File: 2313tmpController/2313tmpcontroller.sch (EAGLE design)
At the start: 32 parts, among them IC1 AT90S2313P, T1 BD139, T2 BD139, T3 BD139, T4 BD139

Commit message: fixed some pads
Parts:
- GNDIN, RSTBTN, VCCIN: device pinhead:PINHD-1X1 -> wirepad:2,54/0,8
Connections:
- net GND: now also GNDIN.P; no longer GNDIN.1
- net N$19: now also RSTBTN.P; no longer RSTBTN.1
- net VCC: now also VCCIN.P; no longer VCCIN.1
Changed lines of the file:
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@@
 <part name="T3" library="transistor" deviceset="BD139" device=""/>
 <part name="T4" library="transistor" deviceset="BD139" device=""/>
-<part name="RSTBTN" library="pinhead" deviceset="PINHD-1X1" device=""/>
 <part name="R5" library="rcl" deviceset="R-EU_" device="0207/7"/>
-<part name="VCCIN" library="pinhead" deviceset="PINHD-1X1" device=""/>
-<part name="GNDIN" library="pinhead" deviceset="PINHD-1X1" device=""/>
 <part name="PAD1" library="wirepad" deviceset="WIREPAD" device="2,15/1,0"/>
 <part name="PAD2" library="wirepad" deviceset="WIREPAD" device="2,15/1,0"/>
@@
 <part name="R6" library="rcl" deviceset="R-EU_" device="0207/7"/>
 <part name="LED1" library="led" deviceset="LED" device="B153"/>
+<part name="VCCIN" library="wirepad" deviceset="2,54/0,8" device=""/>
+<part name="GNDIN" library="wirepad" deviceset="2,54/0,8" device=""/>
+<part name="RSTBTN" library="wirepad" deviceset="2,54/0,8" device=""/>
 </parts>
 <sheets>
@@
 <instance part="T3" gate="G$1" x="119.38" y="-7.62" rot="R270"/>
 <instance part="T4" gate="G$1" x="134.62" y="-7.62" rot="R270"/>
-<instance part="RSTBTN" gate="G$1" x="30.48" y="93.98" rot="R90"/>
 <instance part="R5" gate="G$1" x="43.18" y="88.9" rot="R90"/>
-<instance part="VCCIN" gate="G$1" x="160.02" y="91.44"/>
-<instance part="GNDIN" gate="G$1" x="160.02" y="73.66"/>
 <instance part="PAD1" gate="G$1" x="96.52" y="48.26" rot="R270"/>
 <instance part="PAD2" gate="G$1" x="106.68" y="48.26" rot="R270"/>
@@
 <instance part="R6" gate="G$1" x="116.84" y="96.52" rot="R90"/>
 <instance part="LED1" gate="G$1" x="116.84" y="83.82"/>
+<instance part="VCCIN" gate="P" x="162.56" y="91.44" rot="R180"/>
+<instance part="GNDIN" gate="P" x="162.56" y="73.66" rot="R180"/>
+<instance part="RSTBTN" gate="P" x="30.48" y="96.52" rot="R270"/>
 </instances>
 <busses>
@@
 <segment>
 <pinref part="P+2" gate="VCC" pin="VCC"/>
-<pinref part="VCCIN" gate="G$1" pin="1"/>
 <wire x1="134.62" y1="91.44" x2="134.62" y2="93.98" width="0.1524" layer="91"/>
-<wire x1="157.48" y1="91.44" x2="134.62" y2="91.44" width="0.1524" layer="91"/>
+<wire x1="160.02" y1="91.44" x2="134.62" y2="91.44" width="0.1524" layer="91"/>
 <pinref part="R6" gate="G$1" pin="2"/>
 <wire x1="116.84" y1="101.6" x2="124.46" y2="101.6" width="0.1524" layer="91"/>
@@
 <wire x1="124.46" y1="91.44" x2="134.62" y2="91.44" width="0.1524" layer="91"/>
 <junction x="134.62" y="91.44"/>
+<pinref part="VCCIN" gate="P" pin="P"/>
 </segment>
 </net>
@@
 <segment>
 <pinref part="GND3" gate="1" pin="GND"/>
-<pinref part="GNDIN" gate="G$1" pin="1"/>
 <wire x1="134.62" y1="73.66" x2="134.62" y2="71.12" width="0.1524" layer="91"/>
-<wire x1="157.48" y1="73.66" x2="134.62" y2="73.66" width="0.1524" layer="91"/>
+<wire x1="160.02" y1="73.66" x2="134.62" y2="73.66" width="0.1524" layer="91"/>
 <pinref part="LED1" gate="G$1" pin="C"/>
 <wire x1="116.84" y1="78.74" x2="134.62" y2="78.74" width="0.1524" layer="91"/>
 <wire x1="134.62" y1="78.74" x2="134.62" y2="73.66" width="0.1524" layer="91"/>
 <junction x="134.62" y="73.66"/>
+<pinref part="GNDIN" gate="P" pin="P"/>
 </segment>
 </net>
@@
 <pinref part="R5" gate="G$1" pin="1"/>
 <wire x1="48.26" y1="83.82" x2="43.18" y2="83.82" width="0.1524" layer="91"/>
-<pinref part="RSTBTN" gate="G$1" pin="1"/>
-<wire x1="30.48" y1="91.44" x2="30.48" y2="83.82" width="0.1524" layer="91"/>
+<wire x1="30.48" y1="93.98" x2="30.48" y2="83.82" width="0.1524" layer="91"/>
 <wire x1="30.48" y1="83.82" x2="43.18" y2="83.82" width="0.1524" layer="91"/>
 <junction x="43.18" y="83.82"/>
-</segment>
-</net>
+<pinref part="RSTBTN" gate="P" pin="P"/>
+</segment>
+</net>

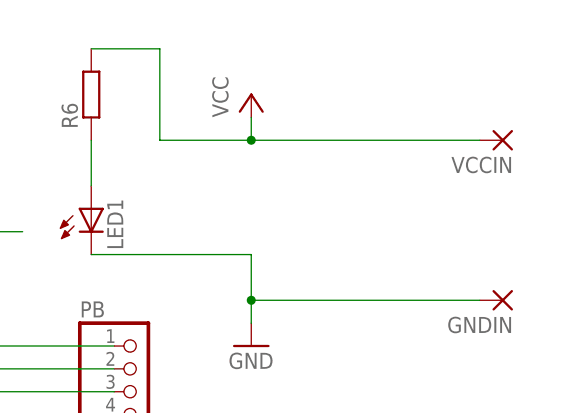
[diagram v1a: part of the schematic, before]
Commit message: added 7805
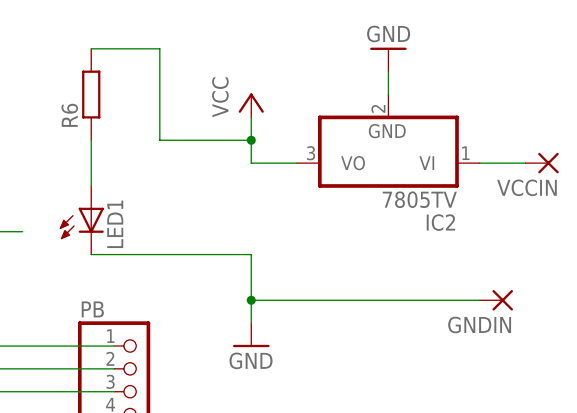
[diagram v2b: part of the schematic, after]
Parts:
- added IC2: 7805TV, linear:7805TV
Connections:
- new net N$33: IC2.VI, VCCIN.P
- net GND: now also IC2.GND
- net VCC: now also IC2.VO; no longer VCCIN.P
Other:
- moved on the sheet: VCCIN
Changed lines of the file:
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@@
 <part name="GNDIN" library="wirepad" deviceset="2,54/0,8" device=""/>
 <part name="RSTBTN" library="wirepad" deviceset="2,54/0,8" device=""/>
+<part name="IC2" library="linear" deviceset="78*" device="TV" technology="05"/>
+<part name="GND4" library="supply1" deviceset="GND" device=""/>
 </parts>
 <sheets>
@@
 <instance part="R6" gate="G$1" x="116.84" y="96.52" rot="R90"/>
 <instance part="LED1" gate="G$1" x="116.84" y="83.82"/>
-<instance part="VCCIN" gate="P" x="162.56" y="91.44" rot="R180"/>
+<instance part="VCCIN" gate="P" x="167.64" y="88.9" rot="R180"/>
 <instance part="GNDIN" gate="P" x="162.56" y="73.66" rot="R180"/>
 <instance part="RSTBTN" gate="P" x="30.48" y="96.52" rot="R270"/>
+<instance part="IC2" gate="A1" x="149.86" y="88.9" rot="R180"/>
+<instance part="GND4" gate="1" x="149.86" y="101.6" rot="R180"/>
 </instances>
 <busses>
@@
 <pinref part="P+2" gate="VCC" pin="VCC"/>
 <wire x1="134.62" y1="91.44" x2="134.62" y2="93.98" width="0.1524" layer="91"/>
-<wire x1="160.02" y1="91.44" x2="134.62" y2="91.44" width="0.1524" layer="91"/>
 <pinref part="R6" gate="G$1" pin="2"/>
 <wire x1="116.84" y1="101.6" x2="124.46" y2="101.6" width="0.1524" layer="91"/>
 <wire x1="124.46" y1="101.6" x2="124.46" y2="91.44" width="0.1524" layer="91"/>
 <wire x1="124.46" y1="91.44" x2="134.62" y2="91.44" width="0.1524" layer="91"/>
+<pinref part="IC2" gate="A1" pin="VO"/>
+<wire x1="139.7" y1="88.9" x2="134.62" y2="88.9" width="0.1524" layer="91"/>
+<wire x1="134.62" y1="88.9" x2="134.62" y2="91.44" width="0.1524" layer="91"/>
 <junction x="134.62" y="91.44"/>
-<pinref part="VCCIN" gate="P" pin="P"/>
 </segment>
 </net>
@@
 <pinref part="GNDIN" gate="P" pin="P"/>
 </segment>
+<segment>
+<pinref part="IC2" gate="A1" pin="GND"/>
+<pinref part="GND4" gate="1" pin="GND"/>
+<wire x1="149.86" y1="96.52" x2="149.86" y2="99.06" width="0.1524" layer="91"/>
+</segment>
 </net>
 <net name="N$1" class="0">
@@
 </segment>
 </net>
+<net name="N$33" class="0">
+<segment>
+<pinref part="IC2" gate="A1" pin="VI"/>
+<pinref part="VCCIN" gate="P" pin="P"/>
+<wire x1="160.02" y1="88.9" x2="165.1" y2="88.9" width="0.1524" layer="91"/>
+</segment>
+</net>
